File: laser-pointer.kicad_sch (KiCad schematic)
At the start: 16 parts, among them Q1 2N7000, U1 TLV272IP, U2 MCP1501-18xCH

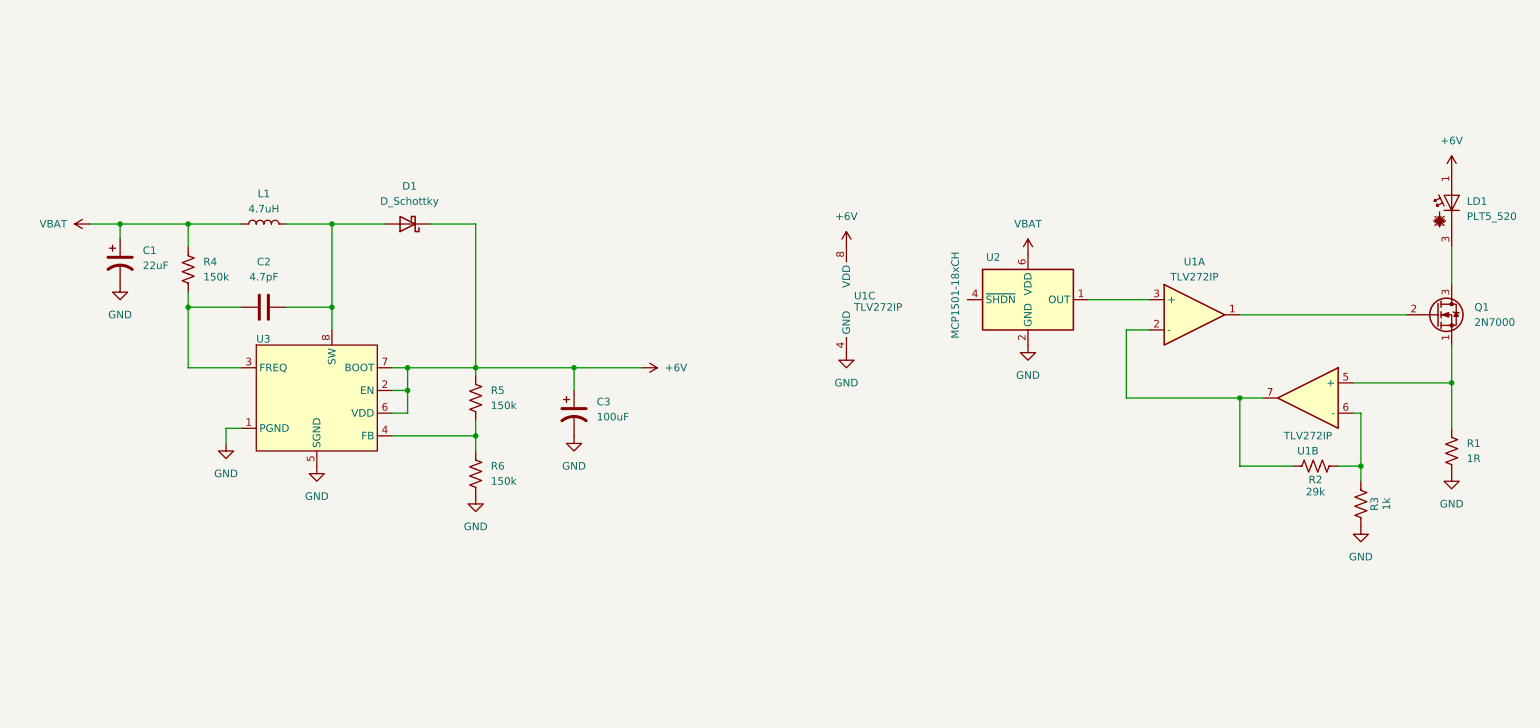
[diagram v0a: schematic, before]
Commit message: Added battery charge controller
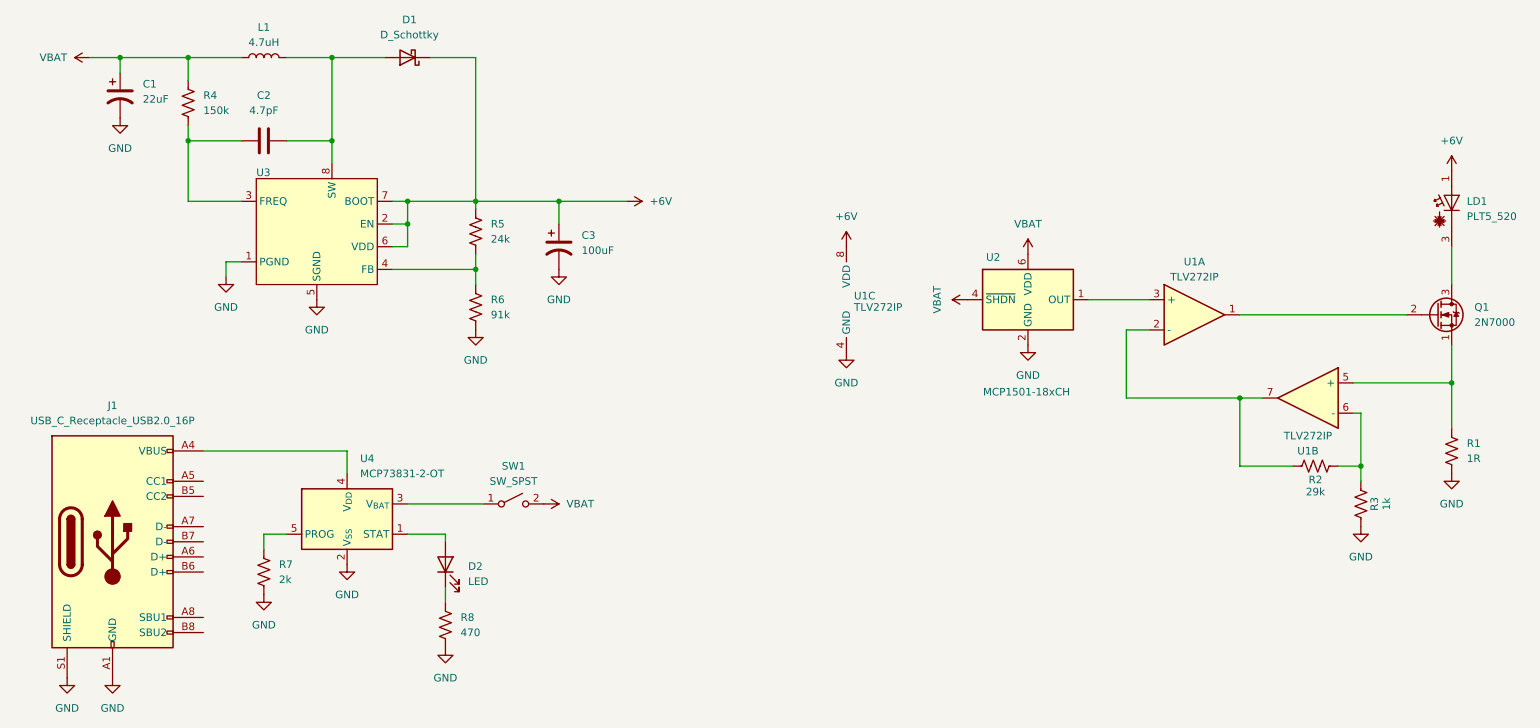
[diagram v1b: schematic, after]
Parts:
- added D2: LED, symbol Device:LED
- added J1: USB_C_Receptacle_USB2.0_16P, Connector_USB:USB_C_Receptacle_GCT_USB4125-xx-x_6P_TopMnt_Horizontal, symbol Connector:USB_C_Receptacle_USB2.0_16P
- added R7: 2k, symbol Device:R_US
- added R8: 470, symbol Device:R_US
- added SW1: SW_SPST, symbol Switch:SW_SPST
- added U4: MCP73831-2-OT, Package_TO_SOT_SMD:SOT-23-5, symbol Battery_Management:MCP73831-2-OT
- R5: value 150k -> 24k
- R6: value 150k -> 91k
- U3: footprint (none) -> Package_SO:VSSOP-8_3x3mm_P0.65mm; Digikey (none) -> https://www.digikey.ca/en/products/detail/texas-instruments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
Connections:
- net GND: now also J1.A1 (GND), J1.A12 (GND), J1.B1 (GND), J1.B12 (GND), J1.S1 (SHIELD), R7.2, R8.2, U4.2 (V_{SS})
- net VBAT: now also U2.4 (~{SHDN}), SW1.2 (B)
- new net: R7.1, U4.5 (PROG)
- new net: SW1.1 (A), U4.3 (V_{BAT})
- new net: D2.1 (K), R8.1
- new net: D2.2 (A), U4.1 (STAT)
- new net: J1.A4 (VBUS), J1.A9 (VBUS), J1.B4 (VBUS), J1.B9 (VBUS), U4.4 (V_{DD})
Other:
- moved on the sheet: C1, C2, C3, D1, L1, R4, R5, R6, U3
